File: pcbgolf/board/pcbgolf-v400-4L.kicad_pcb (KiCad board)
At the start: 2 copper layers, 48.2 x 51 mm, 245 parts, among them J1 DCBARRELSMT, J2 MICRO_SD-0472192001, J3 USB-C-FEMALE, J4 CAN, J5 USB-C-FEMALEGCT, J6 USB-C-FEMALEGCT, J7 USB-C-FEMALEGCT, J8 USB-C-FEMALEGCT, Q1 SIS427-VI, Q2 NFET-DUAL-COMMON-SOURCE-QS5K2, Q3 NFET-DUAL-COMMON-SOURCE-QS5K2, Q4 NFET-DUAL-COMMON-SOURCE-QS5K2, Q5 NFET-DUAL-COMMON-SOURCE-QS5K2, Q6 NFET-DUAL-COMMON-SOURCE-QS5K2, Q7 NFET-DUAL-COMMON-SOURCE-QS5K2, Q8 NFET-DUAL-COMMON-SOURCE-QS5K2, Q9 NFET-DUAL-COMMON-SOURCE-QS5K2, SW1 SPST-2-4PIN, U1 AP62300T, U10 NCS20071XV, U11 NCS20071XV, U12 NCS20071XV, U13 TPS25942, U14 TPS25942, U15 TPS25942, U16 TPS25942, U2 AP62300T, U3 STM32H725ZGTx, U4 USB2517, U5 MCP2542FDT-E/MNY, U6 MCP2542FDT-E/MNY, U7 MCP2542FDT-E/MNY, U8 MCP2542FDT-E/MNY, U9 NCS20071XV, Y1 25MHz, Y2 24MHz

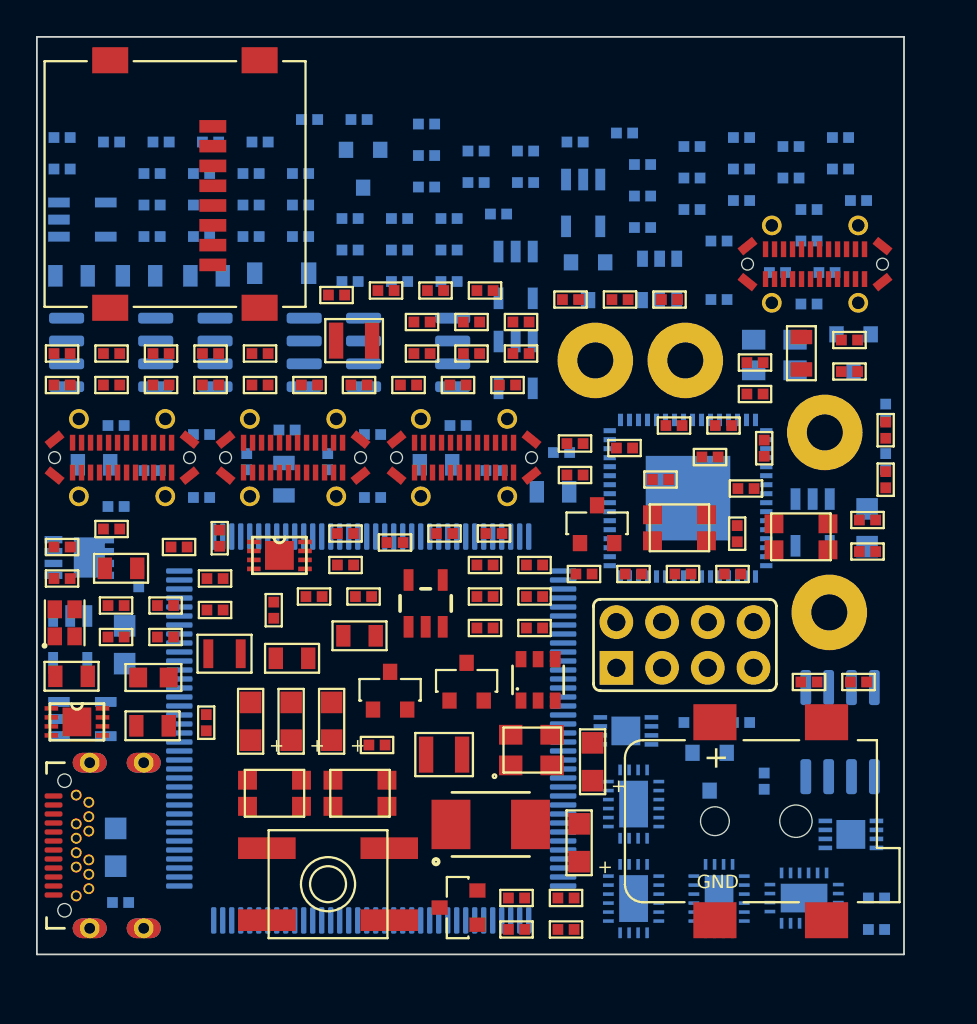
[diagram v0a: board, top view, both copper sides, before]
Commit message: Sync pcbgolf: measured part heights, 3D assembly bounding box, final board
Mirrors lblommesteyn/pcbgolf. The substantive change is that part heights are
now measured from the footprints' own STEP models rather than estimated: the
barrel jack is 11.00 mm, not the 9.00 mm assumed, so Z is 14.35 mm and every
previously reported volume was understated by about 5,300 mm^3.

Also adds bbox3d.py (the real PCBA bounding box, which is what the challenge
scores), step_assembly.py (a STEP built from that same geometry), and the
final LQFP-100 board with R11 not fitted, since the LQFP-100 package has no
PDR_ON pin for it to strap.

Co-Authored-By: Claude Opus 5 <noreply@anthropic.com>
Claude-Session: https://claude.ai/code/session_013nBHDXVrXKghy52w5PgN3h
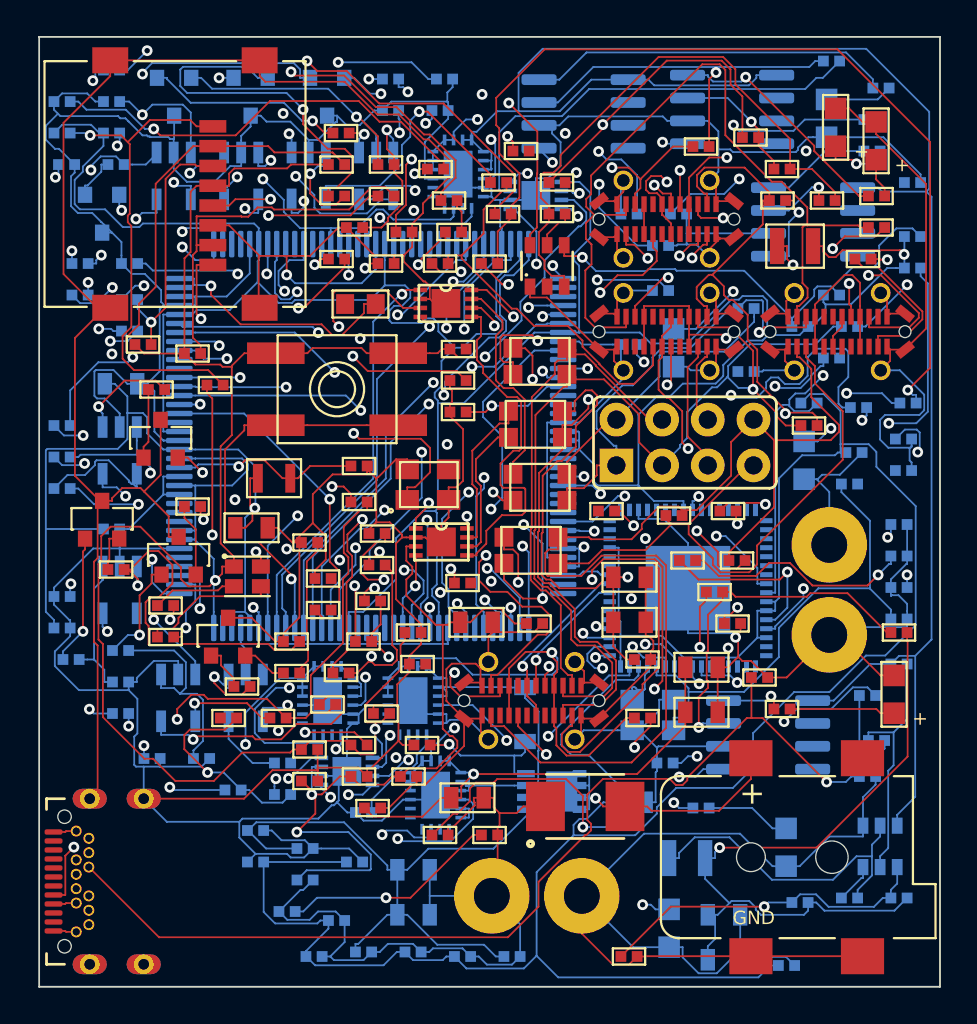
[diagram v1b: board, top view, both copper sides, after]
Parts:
- C11, C24, C31, L2, LED2, LED7, Q6, R119, R87: moved to B.Cu
- C13, C39, R2, R65, R66: moved to F.Cu
- moved C16 51.1 mm to (51.2, 82.5)
- moved C9 50.9 mm to (95.0, 97.5)
- moved C45 50.7 mm to (65.2, 100.8)
- moved R31 48.6 mm to (97.7, 76.8)
- moved C27 48.5 mm to (70.7, 100.5)
- moved C12 48.1 mm to (88.0, 98.5)
- moved LED3 46.3 mm to (94.2, 54.7)
- moved R8 45.7 mm to (96.5, 88.8)
- moved LED15 45.3 mm to (61.7, 53.0)
- moved C48 45.2 mm to (64.7, 94.8)
- moved C1 44.5 mm to (88.0, 101.0)
- moved C35 43.3 mm to (63.7, 98.3), turned to 0 degrees
- moved U14 42.8 mm to (73.2, 57.3)
- moved R119 42.8 mm to (94.0, 67.5)
- moved LED2 42.5 mm to (93.7, 54.2)
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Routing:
- net GND: track 0.00 -> 860.5 mm, vias 0 -> 2
- net +3V3: track 0.00 -> 496.1 mm, vias 0 -> 4
- net +5V: track 0.00 -> 251.6 mm, vias 0 -> 4
- net +12V: track 0.00 -> 187.9 mm, vias 0 -> 1
- net N$9: track 0.00 -> 138.5 mm, vias 0 -> 3
- net CH1_IMON: track 0.00 -> 130.9 mm, vias 0 -> 3
- net CAN0_L: track 0.00 -> 111.7 mm, vias 0 -> 4
- net N$237: track 0.00 -> 107.0 mm, vias 0 -> 3
- net CH2_SBU1_IGN: track 0.00 -> 100.9 mm, vias 0 -> 3
- net CAN3_H: track 0.00 -> 93.1 mm, vias 0 -> 1
- net CH2_SBU1_RELAY: track 0.00 -> 92.9 mm, vias 0 -> 3
- net CH4_SBU2: track 0.00 -> 92.2 mm, vias 0 -> 2
- net VDDLDO: track 0.00 -> 91.9 mm, vias 0 -> 3
- net CAN1_L: track 0.00 -> 87.7 mm, vias 0 -> 3
- net CAN0_H: track 0.00 -> 86.8 mm, vias 0 -> 1
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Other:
- board size 48.2 x 51 mm -> 50 x 52.8 mm
- copper layers 2 -> 4
